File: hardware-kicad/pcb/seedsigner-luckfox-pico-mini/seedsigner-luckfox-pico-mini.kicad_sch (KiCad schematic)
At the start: 37 parts, among them J1 Conn_01x10, J2 Conn_01x05, U1 LuckFox_Pico_PLUS_PRO, U2 RASPBERRY_PI_3_MODEL_B+

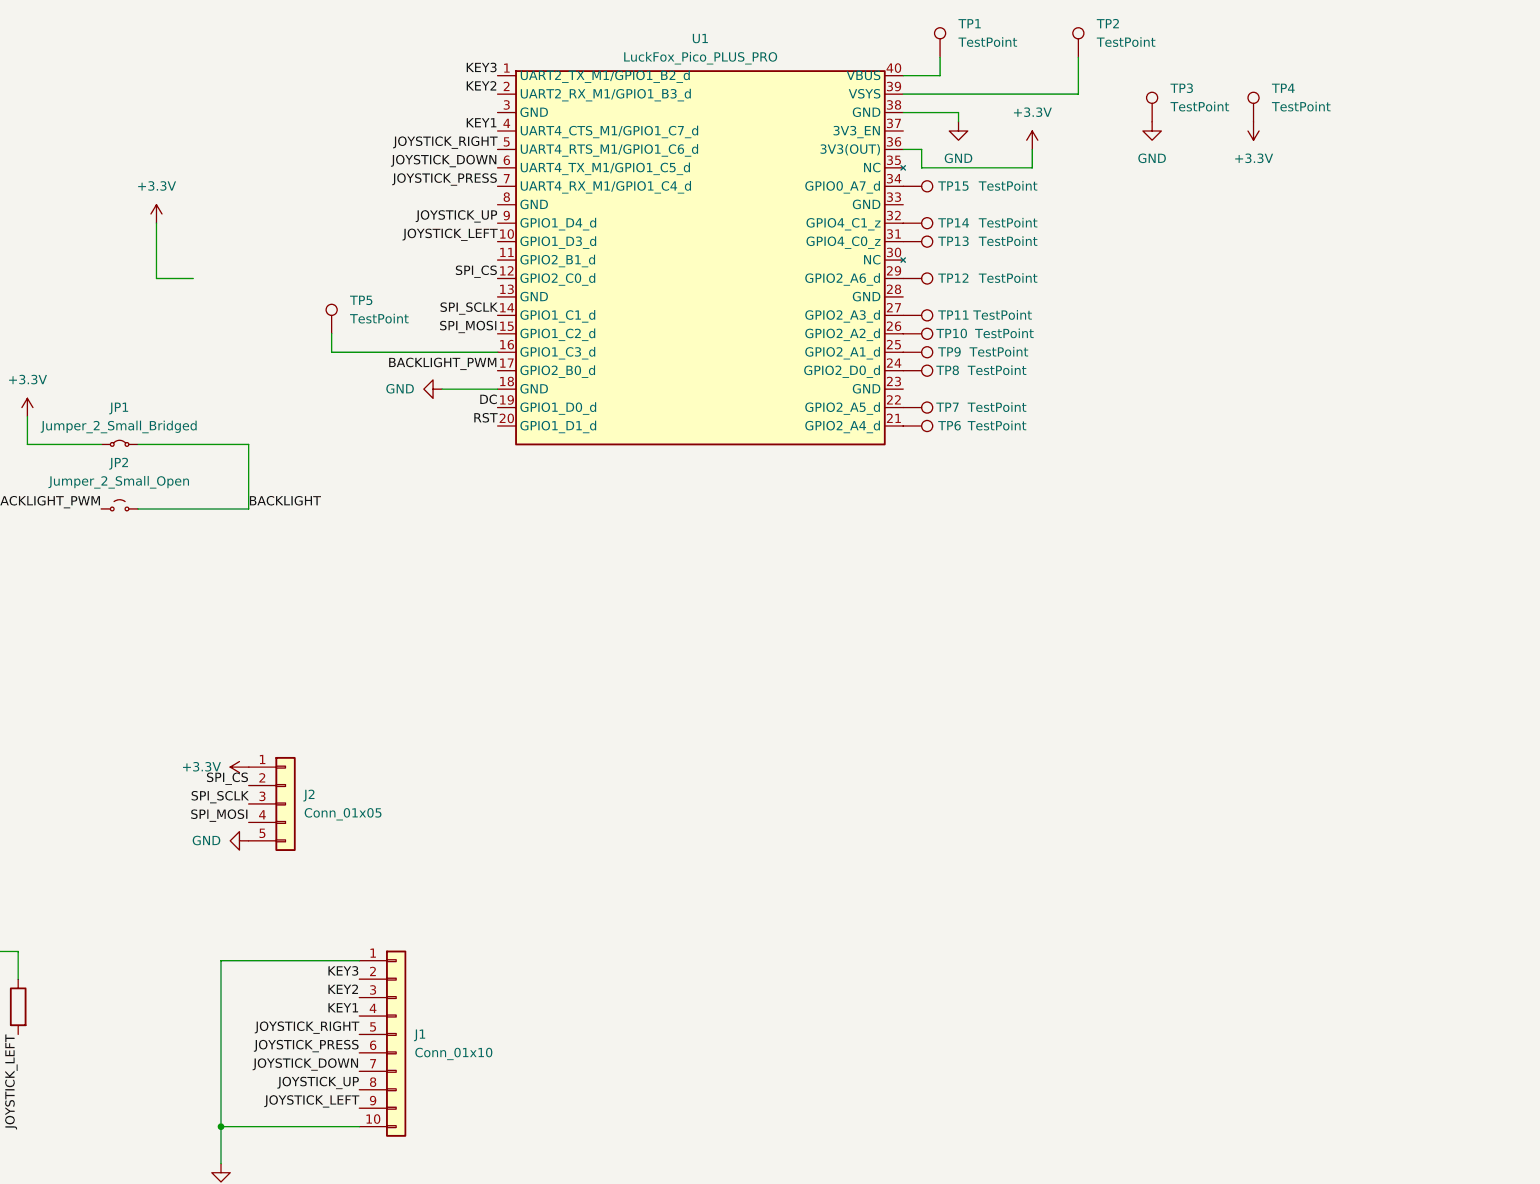
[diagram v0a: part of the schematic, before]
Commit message: restructure dir structure and start luckfox-pico-mini pcb
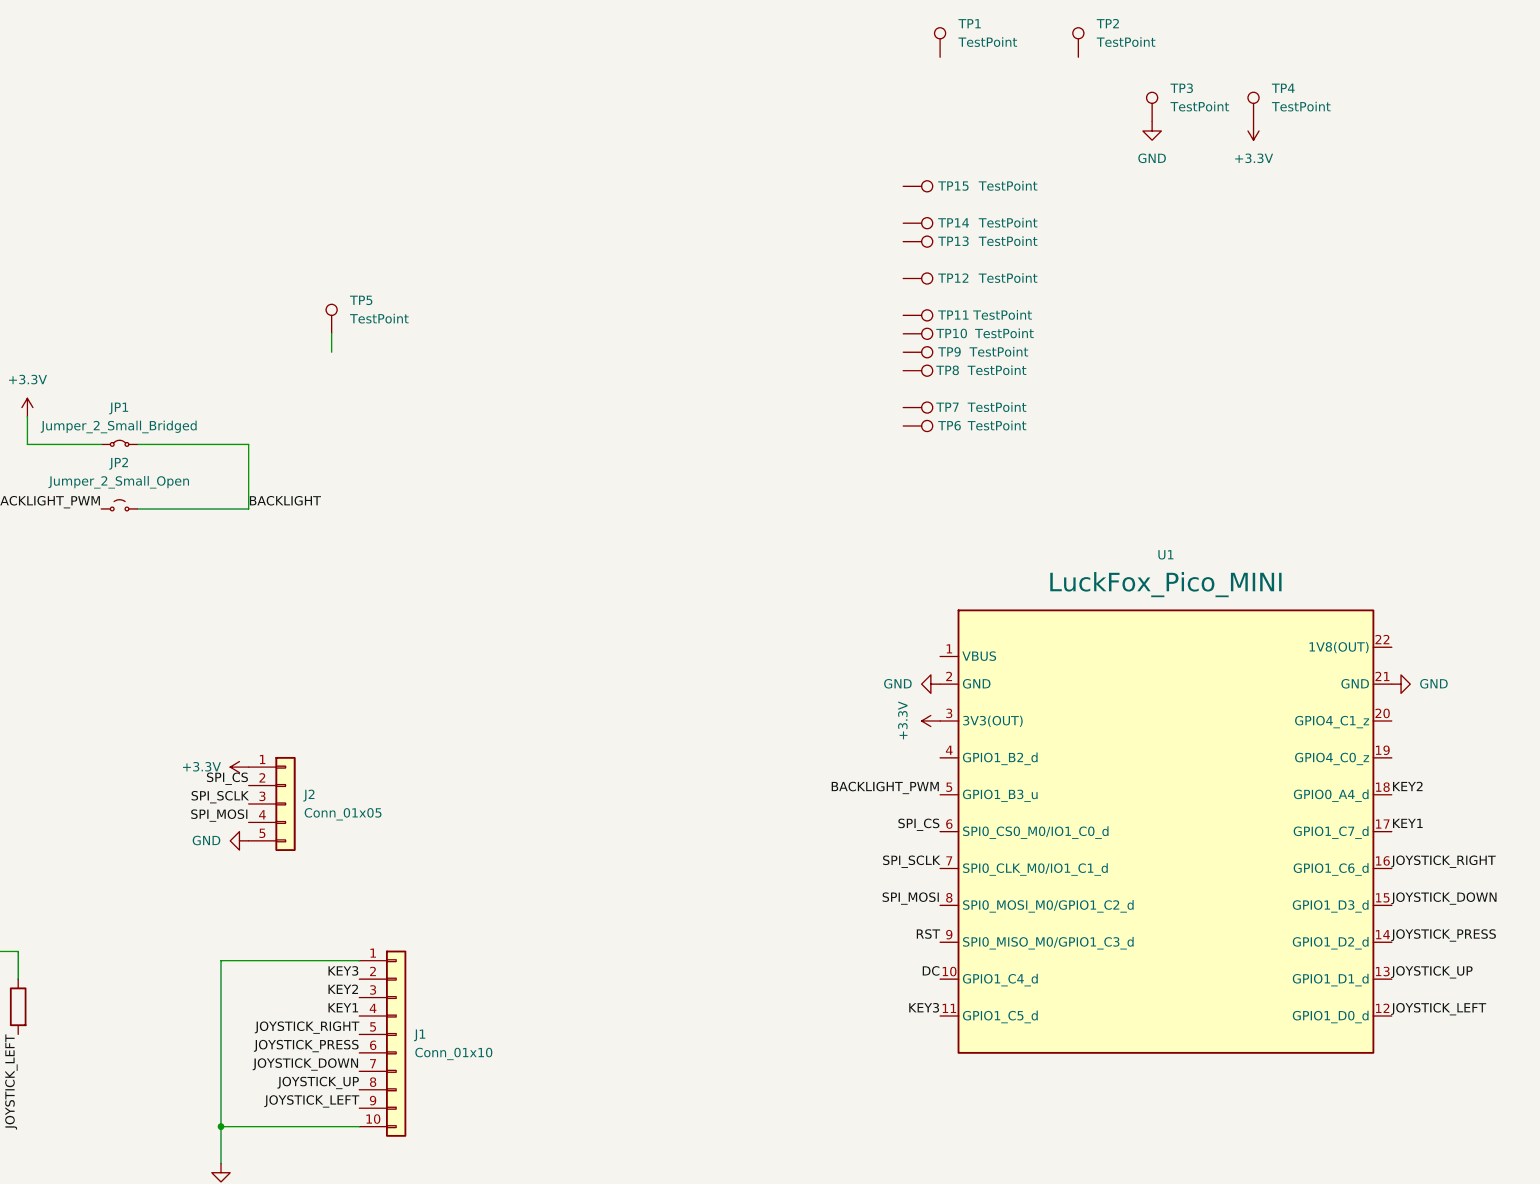
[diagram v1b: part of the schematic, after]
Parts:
- removed U1: LuckFox_Pico_PLUS_PRO, seedsigner-luckfox:LUCKFOX_PICO_PRO_MAX_PTH, symbol Luckfox:LuckFox_Pico_PLUS_PRO
- added U1: LuckFox_Pico_MINI, luckfox:LUCKFOX_PICO_MINI, symbol Luckfox:LuckFox_Pico_MINI
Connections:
- net +3.3V: now also U1.3 (3V3(OUT))
- net BACKLIGHT_PWM: now also U1.5 (GPIO1_B3_u)
- net DC: now also U1.10 (GPIO1_C4_d)
- net GND: now also U1.2 (GND), U1.21 (GND)
- net JOYSTICK_DOWN: now also U1.15 (GPIO1_D3_d)
- net JOYSTICK_LEFT: now also U1.12 (GPIO1_D0_d)
- net JOYSTICK_PRESS: now also U1.14 (GPIO1_D2_d)
- net JOYSTICK_RIGHT: now also U1.16 (GPIO1_C6_d)
- net JOYSTICK_UP: now also U1.13 (GPIO1_D1_d)
- net KEY1: now also U1.17 (GPIO1_C7_d)
- net KEY2: now also U1.18 (GPIO0_A4_d)
- net KEY3: now also U1.11 (GPIO1_C5_d)
- net RST: now also U1.9 (SPI0_MISO_M0/GPIO1_C3_d)
- net SPI_CS: now also U1.6 (SPI0_CS0_M0/IO1_C0_d)
- net SPI_MOSI: now also U1.8 (SPI0_MOSI_M0/GPIO1_C2_d)
- net SPI_SCLK: now also U1.7 (SPI0_CLK_M0/IO1_C1_d)

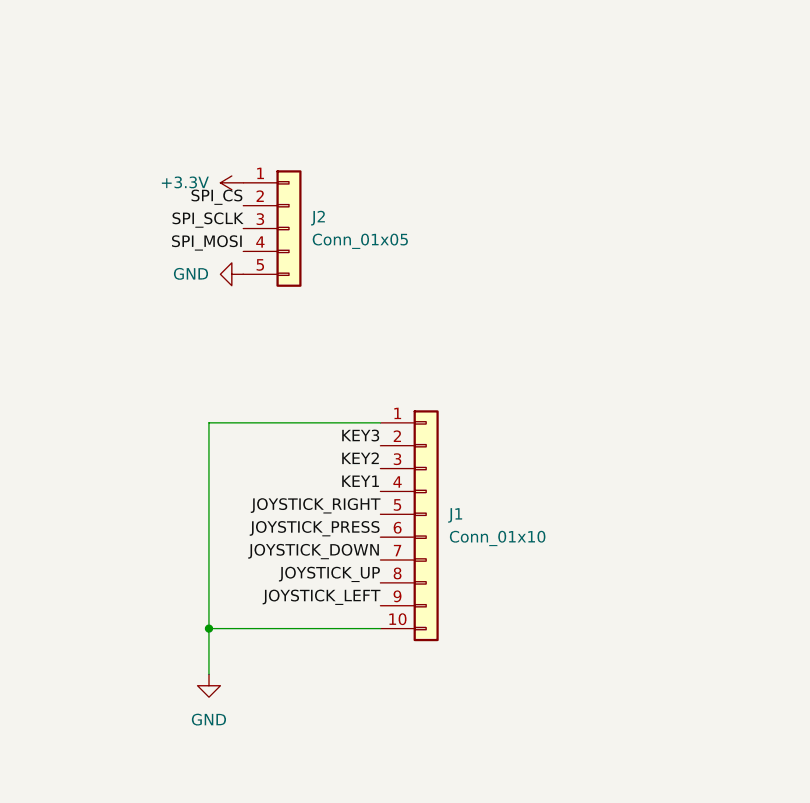
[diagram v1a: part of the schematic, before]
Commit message: add waveshare lcd 3d model and initial pcb routing
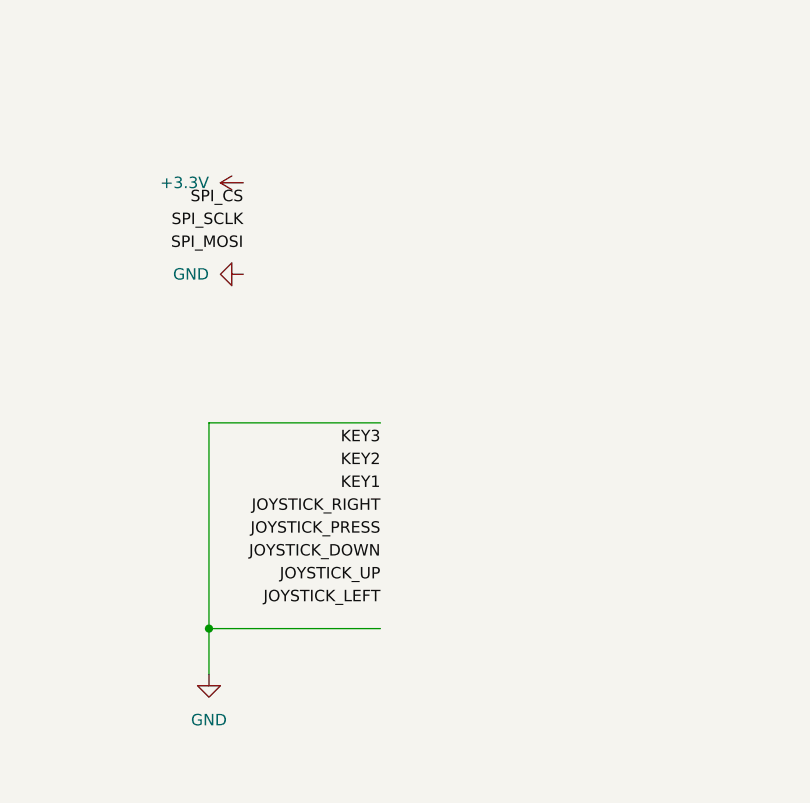
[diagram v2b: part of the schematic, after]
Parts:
- removed J1: Conn_01x10, seedsigner-luckfox:PinHeader_1x10_P2.54mm_Horizontal, symbol Connector_Generic:Conn_01x10
- removed J2: Conn_01x05, seedsigner-luckfox:PinHeader_1x05_P2.54mm_Horizontal, symbol Connector_Generic:Conn_01x05
- R1, R2, R3, R4, R5, R6, R7, R8: footprint seedsigner-luckfox:R_2512_6332Metric -> Resistor_SMD:R_0603_1608Metric_Pad0.98x0.95mm_HandSolder
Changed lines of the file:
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@@
 			)
 		)
-		(property "Footprint" "seedsigner-luckfox:R_2512_6332Metric"
+		(property "Footprint" "Resistor_SMD:R_0603_1608Metric_Pad0.98x0.95mm_HandSolder"
 			(at 137.668 160.02 90)
 			(effects
@@
 				(path "/dd9f0a7b-8b90-4e47-9769-d29b64af2c20"
 					(reference "R3")
-					(unit 1)
-				)
-			)
-		)
-	)
-	(symbol
-		(lib_id "Connector_Generic:Conn_01x10")
-		(at 219.71 163.83 0)
-		(unit 1)
-		(exclude_from_sim no)
-		(in_bom yes)
-		(on_board yes)
-		(dnp no)
-		(fields_autoplaced yes)
-		(property "Reference" "J1"
-			(at 222.25 163.8299 0)
-			(effects
-				(font
-					(size 1.27 1.27)
-				)
-				(justify left)
-			)
-		)
-		(property "Value" "Conn_01x10"
-			(at 222.25 166.3699 0)
-			(effects
-				(font
-					(size 1.27 1.27)
-				)
-				(justify left)
-			)
-		)
-		(property "Footprint" "seedsigner-luckfox:PinHeader_1x10_P2.54mm_Horizontal"
-			(at 219.71 163.83 0)
-			(effects
-				(font
-					(size 1.27 1.27)
-				)
-				(hide yes)
-			)
-		)
-		(property "Datasheet" "~"
-			(at 219.71 163.83 0)
-			(effects
-				(font
-					(size 1.27 1.27)
-				)
-				(hide yes)
-			)
-		)
-		(property "Description" "Generic connector, single row, 01x10, script generated (kicad-library-utils/schlib/autogen/connector/)"
-			(at 219.71 163.83 0)
-			(effects
-				(font
-					(size 1.27 1.27)
-				)
-				(hide yes)
-			)
-		)
-		(pin "4"
-		)
-		(pin "10"
-		)
-		(pin "8"
-		)
-		(pin "7"
-		)
-		(pin "1"
-		)
-		(pin "3"
-		)
-		(pin "9"
-		)
-		(pin "2"
-		)
-		(pin "5"
-		)
-		(pin "6"
-		)
-		(instances
-			(project ""
-				(path "/dd9f0a7b-8b90-4e47-9769-d29b64af2c20"
-					(reference "J1")
 					(unit 1)
 				)
@@
 			)
 		)
-		(property "Footprint" "seedsigner-luckfox:R_2512_6332Metric"
+		(property "Footprint" "Resistor_SMD:R_0603_1608Metric_Pad0.98x0.95mm_HandSolder"
 			(at 169.418 160.02 90)
 			(effects
@@
 			)
 		)
-		(property "Footprint" "seedsigner-luckfox:R_2512_6332Metric"
+		(property "Footprint" "Resistor_SMD:R_0603_1608Metric_Pad0.98x0.95mm_HandSolder"
 			(at 131.318 160.02 90)
 			(effects
@@
 			)
 		)
-		(property "Footprint" "seedsigner-luckfox:R_2512_6332Metric"
+		(property "Footprint" "Resistor_SMD:R_0603_1608Metric_Pad0.98x0.95mm_HandSolder"
 			(at 163.068 160.02 90)
 			(effects
@@
 			)
 		)
-		(property "Footprint" "seedsigner-luckfox:R_2512_6332Metric"
+		(property "Footprint" "Resistor_SMD:R_0603_1608Metric_Pad0.98x0.95mm_HandSolder"
 			(at 144.018 160.02 90)
 			(effects
@@
 				(path "/dd9f0a7b-8b90-4e47-9769-d29b64af2c20"
 					(reference "#PWR012")
-					(unit 1)
-				)
-			)
-		)
-	)
-	(symbol
-		(lib_id "Connector_Generic:Conn_01x05")
-		(at 204.47 132.08 0)
-		(unit 1)
-		(exclude_from_sim no)
-		(in_bom yes)
-		(on_board yes)
-		(dnp no)
-		(fields_autoplaced yes)
-		(property "Reference" "J2"
-			(at 207.01 130.8099 0)
-			(effects
-				(font
-					(size 1.27 1.27)
-				)
-				(justify left)
-			)
-		)
-		(property "Value" "Conn_01x05"
-			(at 207.01 133.3499 0)
-			(effects
-				(font
-					(size 1.27 1.27)
-				)
-				(justify left)
-			)
-		)
-		(property "Footprint" "seedsigner-luckfox:PinHeader_1x05_P2.54mm_Horizontal"
-			(at 204.47 132.08 0)
-			(effects
-				(font
-					(size 1.27 1.27)
-				)
-				(hide yes)
-			)
-		)
-		(property "Datasheet" "~"
-			(at 204.47 132.08 0)
-			(effects
-				(font
-					(size 1.27 1.27)
-				)
-				(hide yes)
-			)
-		)
-		(property "Description" "Generic connector, single row, 01x05, script generated (kicad-library-utils/schlib/autogen/connector/)"
-			(at 204.47 132.08 0)
-			(effects
-				(font
-					(size 1.27 1.27)
-				)
-				(hide yes)
-			)
-		)
-		(pin "4"
-		)
-		(pin "5"
-		)
-		(pin "3"
-		)
-		(pin "2"
-		)
-		(pin "1"
-		)
-		(instances
-			(project ""
-				(path "/dd9f0a7b-8b90-4e47-9769-d29b64af2c20"
-					(reference "J2")
 					(unit 1)
 				)
@@
 			)
 		)
-		(property "Footprint" "seedsigner-luckfox:R_2512_6332Metric"
+		(property "Footprint" "Resistor_SMD:R_0603_1608Metric_Pad0.98x0.95mm_HandSolder"
 			(at 156.718 160.02 90)
 			(effects
@@
 			)
 		)
-		(property "Footprint" "seedsigner-luckfox:R_2512_6332Metric"
+		(property "Footprint" "Resistor_SMD:R_0603_1608Metric_Pad0.98x0.95mm_HandSolder"
 			(at 150.368 160.02 90)
 			(effects
@@
 			)
 		)
-		(property "Footprint" "seedsigner-luckfox:R_2512_6332Metric"
+		(property "Footprint" "Resistor_SMD:R_0603_1608Metric_Pad0.98x0.95mm_HandSolder"
 			(at 124.968 160.02 90)
 			(effects

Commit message: auto-route and cleanup of pico mini devboard
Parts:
- removed TP1, TP10, TP11, TP12, TP13, TP14, TP15, TP2, TP5, TP6, TP7, TP8, TP9: TestPoint, seedsigner-luckfox:TestPoint_Pad_1.5x1.5mm, symbol Connector:TestPoint
- U1: footprint luckfox:LUCKFOX_PICO_MINI -> seedsigner-luckfox:LUCKFOX_PICO_MINI
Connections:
- net +3.3V: now also JP2.1 (A); no longer JP1.1 (A)
- net BACKLIGHT_PWM: now also JP1.1 (A); no longer JP2.1 (A)
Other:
- moved on the sheet: JP1, JP2
